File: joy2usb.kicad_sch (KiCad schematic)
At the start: 16 parts, among them J1 DB9_Male, J2 Conn_02x04_Odd_Even, SW1 RST, SW2 SW_SPDT, U1 Arduino_Pro_Micro, U2 4066

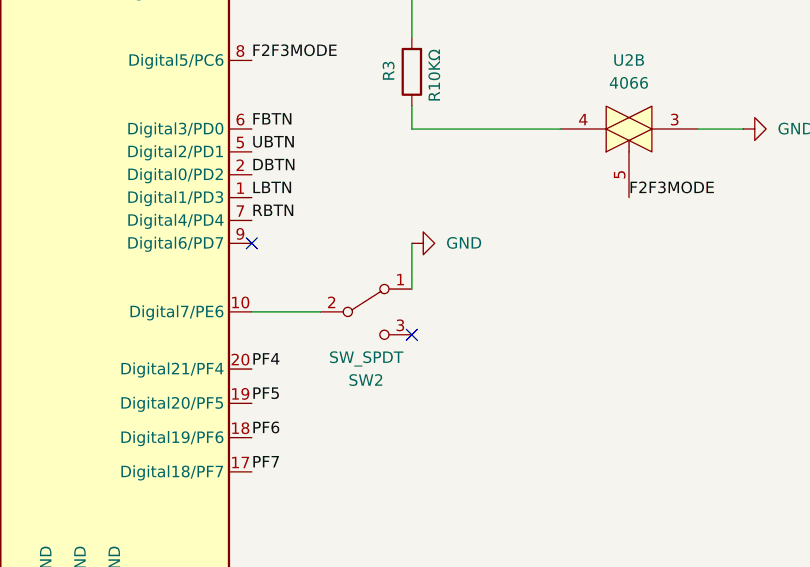
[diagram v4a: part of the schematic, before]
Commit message: PCB Rev. 4.0
update C64/Amiga switch
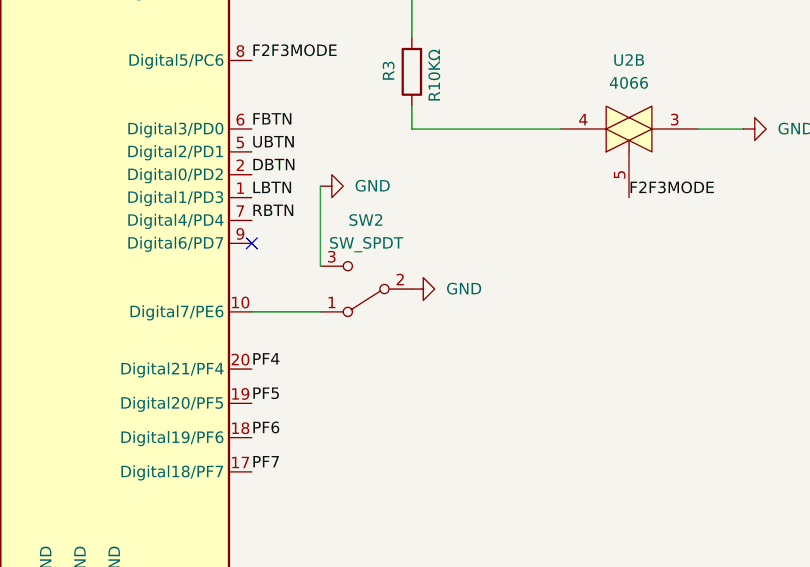
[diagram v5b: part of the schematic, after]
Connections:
- net GND: now also SW2.2 (B), SW2.3 (C); no longer SW2.1 (A)
- net at U1.10 (Digital7/PE6): now also SW2.1 (A); no longer SW2.2 (B)
- no-connect marks 7 -> 6
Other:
- moved on the sheet: SW2
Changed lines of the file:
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@@
   (title_block
     (title "joy2usb")
-    (rev "3.0")
+    (rev "4.0")
     (company "mistepien@wp.pl")
   )
@@
   (no_connect (at 111.76 55.88))
   (no_connect (at 111.76 91.44))
-  (no_connect (at 129.54 101.6))
   (no_connect (at 111.76 58.42))
   (no_connect (at 81.28 55.88))
@@
     (stroke (width 0) (type default) (color 0 0 0 0))
   )
-  (wire (pts (xy 129.54 91.44) (xy 129.54 96.52))
-    (stroke (width 0) (type default) (color 0 0 0 0))
-  )
   (wire (pts (xy 211.455 106.045) (xy 212.725 106.045))
     (stroke (width 0) (type default) (color 0 0 0 0))
@@
   )
   (wire (pts (xy 220.345 106.045) (xy 225.425 106.045))
+    (stroke (width 0) (type default) (color 0 0 0 0))
+  )
+  (wire (pts (xy 119.38 85.09) (xy 119.38 93.98))
     (stroke (width 0) (type default) (color 0 0 0 0))
   )
@@
     (pin "1")
   )
-  (symbol (lib_id "power:GND") (at 129.54 91.44 90) (unit 1)
-    (in_bom yes) (on_board yes) (fields_autoplaced)
-    (property "Reference" "#PWR0107" (id 0) (at 135.89 91.44 0)
-      (effects (font (size 1.27 1.27)) hide)
-    )
-    (property "Value" "GND" (id 1) (at 133.35 91.4399 90)
-      (effects (font (size 1.27 1.27)) (justify right))
-    )
-    (property "Footprint" "" (id 2) (at 129.54 91.44 0)
-      (effects (font (size 1.27 1.27)) hide)
-    )
-    (property "Datasheet" "" (id 3) (at 129.54 91.44 0)
-      (effects (font (size 1.27 1.27)) hide)
-    )
-    (pin "1")
-  )
   (symbol (lib_id "Mechanical:MountingHole") (at 137.795 181.61 0) (unit 1)
     (in_bom no) (on_board yes)
@@
     (pin "1")
   )
-  (symbol (lib_id "Switch:SW_SPDT") (at 124.46 99.06 0) (unit 1)
-    (in_bom yes) (on_board yes) (fields_autoplaced)
-    (property "Reference" "SW2" (id 0) (at 124.46 106.68 0))
-    (property "Value" "SW_SPDT" (id 1) (at 124.46 104.14 0))
-    (property "Footprint" "Misc:MFP_1220_KNITTER_SWITCH_SPDT_Oval" (id 2) (at 124.46 99.06 0)
-      (effects (font (size 1.27 1.27)) hide)
-    )
-    (property "Datasheet" "~" (id 3) (at 124.46 99.06 0)
+  (symbol (lib_id "Switch:SW_SPDT") (at 124.46 96.52 180) (unit 1)
+    (in_bom yes) (on_board yes) (fields_autoplaced)
+    (property "Reference" "SW2" (id 0) (at 124.46 88.9 0))
+    (property "Value" "SW_SPDT" (id 1) (at 124.46 91.44 0))
+    (property "Footprint" "Misc:MFP_1220_KNITTER_SWITCH_SPDT_Oval" (id 2) (at 124.46 96.52 0)
+      (effects (font (size 1.27 1.27)) hide)
+    )
+    (property "Datasheet" "~" (id 3) (at 124.46 96.52 0)
       (effects (font (size 1.27 1.27)) hide)
     )
@@
     (pin "1")
   )
-  (symbol (lib_id "power:VCC") (at 133.35 180.34 0) (unit 1)
-    (in_bom yes) (on_board yes) (fields_autoplaced)
-    (property "Reference" "#PWR023" (id 0) (at 133.35 184.15 0)
-      (effects (font (size 1.27 1.27)) hide)
-    )
-    (property "Value" "VCC" (id 1) (at 133.35 175.26 0))
-    (property "Footprint" "" (id 2) (at 133.35 180.34 0)
-      (effects (font (size 1.27 1.27)) hide)
-    )
-    (property "Datasheet" "" (id 3) (at 133.35 180.34 0)
-      (effects (font (size 1.27 1.27)) hide)
-    )
-    (pin "1")
-  )
   (symbol (lib_id "Device:LED") (at 216.535 106.045 180) (unit 1)
     (in_bom yes) (on_board yes) (fields_autoplaced)
@@
     )
     (property "Datasheet" "" (id 3) (at 92.71 137.16 0)
+      (effects (font (size 1.27 1.27)) hide)
+    )
+    (pin "1")
+  )
+  (symbol (lib_id "power:GND") (at 129.54 96.52 90) (unit 1)
+    (in_bom yes) (on_board yes) (fields_autoplaced)
+    (property "Reference" "#PWR0107" (id 0) (at 135.89 96.52 0)
+      (effects (font (size 1.27 1.27)) hide)
+    )
+    (property "Value" "GND" (id 1) (at 133.35 96.5199 90)
+      (effects (font (size 1.27 1.27)) (justify right))
+    )
+    (property "Footprint" "" (id 2) (at 129.54 96.52 0)
+      (effects (font (size 1.27 1.27)) hide)
+    )
+    (property "Datasheet" "" (id 3) (at 129.54 96.52 0)
       (effects (font (size 1.27 1.27)) hide)
     )
@@
     (pin "8")
   )
+  (symbol (lib_id "power:GND") (at 119.38 85.09 90) (unit 1)
+    (in_bom yes) (on_board yes) (fields_autoplaced)
+    (property "Reference" "#PWR02" (id 0) (at 125.73 85.09 0)
+      (effects (font (size 1.27 1.27)) hide)
+    )
+    (property "Value" "GND" (id 1) (at 123.19 85.0899 90)
+      (effects (font (size 1.27 1.27)) (justify right))
+    )
+    (property "Footprint" "" (id 2) (at 119.38 85.09 0)
+      (effects (font (size 1.27 1.27)) hide)
+    )
+    (property "Datasheet" "" (id 3) (at 119.38 85.09 0)
+      (effects (font (size 1.27 1.27)) hide)
+    )
+    (pin "1")
+  )
   (symbol (lib_id "power:GND") (at 33.02 128.27 180) (unit 1)
     (in_bom yes) (on_board yes) (fields_autoplaced)
@@
     )
   )
+  (symbol (lib_id "power:VCC") (at 133.35 180.34 0) (unit 1)
+    (in_bom yes) (on_board yes) (fields_autoplaced)
+    (property "Reference" "#PWR0117" (id 0) (at 133.35 184.15 0)
+      (effects (font (size 1.27 1.27)) hide)
+    )
+    (property "Value" "VCC" (id 1) (at 133.35 175.26 0))
+    (property "Footprint" "" (id 2) (at 133.35 180.34 0)
+      (effects (font (size 1.27 1.27)) hide)
+    )
+    (property "Datasheet" "" (id 3) (at 133.35 180.34 0)
+      (effects (font (size 1.27 1.27)) hide)
+    )
+    (pin "1")
+  )
   (symbol (lib_id "Mechanical:MountingHole") (at 137.795 190.5 0) (unit 1)
     (in_bom no) (on_board yes)
@@
       (reference "#PWR01") (unit 1) (value "VCC") (footprint "")
     )
+    (path "/b360e194-d5b5-4145-87b4-c475cf3ef423"
+      (reference "#PWR02") (unit 1) (value "GND") (footprint "")
+    )
     (path "/9b6d3cc9-8699-4512-8b17-ada5ebf54a78"
       (reference "#PWR03") (unit 1) (value "VCC") (footprint "")
@@
       (reference "#PWR017") (unit 1) (value "VCC") (footprint "")
     )
-    (path "/3df7e21b-5810-4bcd-8937-5da3a9ffe577"
-      (reference "#PWR023") (unit 1) (value "VCC") (footprint "")
-    )
     (path "/0826918b-c24e-40db-a768-35c3e120095f"
       (reference "#PWR0101") (unit 1) (value "VCC") (footprint "")
@@
       (reference "#PWR0106") (unit 1) (value "GND") (footprint "")
     )
-    (path "/084083df-fdf8-459b-b91f-12f5dfdc3fca"
+    (path "/53eb5098-0697-4345-8a1e-de4578279585"
       (reference "#PWR0107") (unit 1) (value "GND") (footprint "")
     )
@@
       (reference "#PWR0116") (unit 1) (value "GND") (footprint "")
     )
+    (path "/c125f043-00b6-4dfd-8738-0b01be89b4c8"
+      (reference "#PWR0117") (unit 1) (value "VCC") (footprint "")
+    )
     (path "/fed0e2ac-5eb0-44b8-8f14-4abe77bb9479"

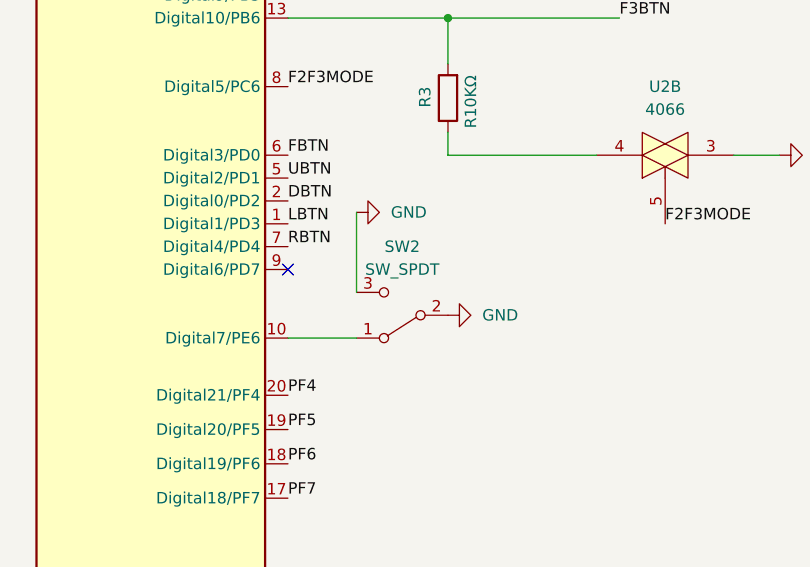
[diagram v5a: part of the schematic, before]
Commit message: PCB Rev. 4.1
SW2 minor amendment
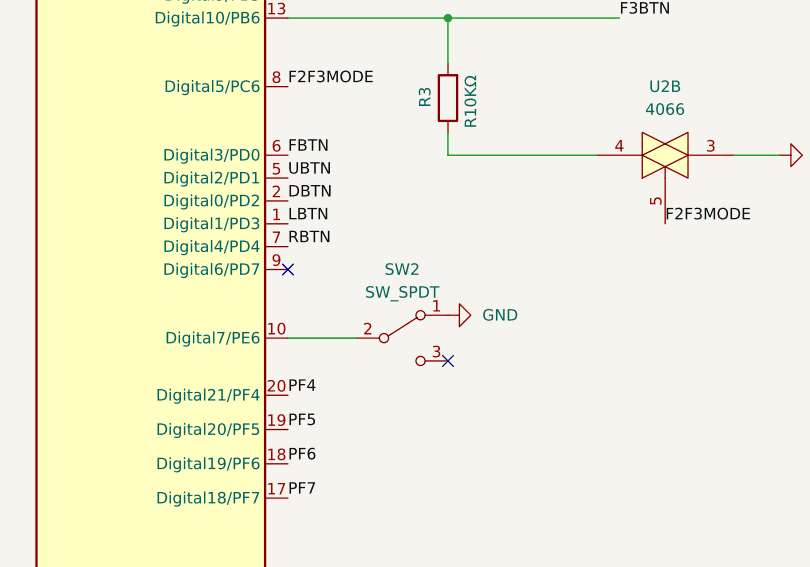
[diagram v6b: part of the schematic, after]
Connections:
- net GND: now also SW2.1 (A); no longer SW2.2 (B), SW2.3 (C)
- net at U1.10 (Digital7/PE6): now also SW2.2 (B); no longer SW2.1 (A)
- no-connect marks 6 -> 7
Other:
- moved on the sheet: SW2
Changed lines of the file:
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@@
   (title_block
     (title "joy2usb")
-    (rev "4.0")
+    (rev "4.1")
     (company "mistepien@wp.pl")
   )
@@
   (no_connect (at 81.28 55.88))
   (no_connect (at 111.76 50.8))
+  (no_connect (at 129.54 101.6))
   (wire (pts (xy 231.14 48.26) (xy 238.76 48.26))
     (stroke (width 0) (type default) (color 0 0 0 0))
@@
   )
   (wire (pts (xy 220.345 106.045) (xy 225.425 106.045))
-    (stroke (width 0) (type default) (color 0 0 0 0))
-  )
-  (wire (pts (xy 119.38 85.09) (xy 119.38 93.98))
     (stroke (width 0) (type default) (color 0 0 0 0))
   )
@@
     (pin "1")
   )
-  (symbol (lib_id "Switch:SW_SPDT") (at 124.46 96.52 180) (unit 1)
-    (in_bom yes) (on_board yes) (fields_autoplaced)
-    (property "Reference" "SW2" (id 0) (at 124.46 88.9 0))
-    (property "Value" "SW_SPDT" (id 1) (at 124.46 91.44 0))
-    (property "Footprint" "Misc:MFP_1220_KNITTER_SWITCH_SPDT_Oval" (id 2) (at 124.46 96.52 0)
-      (effects (font (size 1.27 1.27)) hide)
-    )
-    (property "Datasheet" "~" (id 3) (at 124.46 96.52 0)
+  (symbol (lib_id "Switch:SW_SPDT") (at 124.46 99.06 0) (unit 1)
+    (in_bom yes) (on_board yes) (fields_autoplaced)
+    (property "Reference" "SW2" (id 0) (at 124.46 91.44 0))
+    (property "Value" "SW_SPDT" (id 1) (at 124.46 93.98 0))
+    (property "Footprint" "Misc:MFP_1220_KNITTER_SWITCH_SPDT_Oval" (id 2) (at 124.46 99.06 0)
+      (effects (font (size 1.27 1.27)) hide)
+    )
+    (property "Datasheet" "~" (id 3) (at 124.46 99.06 0)
       (effects (font (size 1.27 1.27)) hide)
     )
@@
     (pin "8")
   )
-  (symbol (lib_id "power:GND") (at 119.38 85.09 90) (unit 1)
-    (in_bom yes) (on_board yes) (fields_autoplaced)
-    (property "Reference" "#PWR02" (id 0) (at 125.73 85.09 0)
-      (effects (font (size 1.27 1.27)) hide)
-    )
-    (property "Value" "GND" (id 1) (at 123.19 85.0899 90)
-      (effects (font (size 1.27 1.27)) (justify right))
-    )
-    (property "Footprint" "" (id 2) (at 119.38 85.09 0)
-      (effects (font (size 1.27 1.27)) hide)
-    )
-    (property "Datasheet" "" (id 3) (at 119.38 85.09 0)
-      (effects (font (size 1.27 1.27)) hide)
-    )
-    (pin "1")
-  )
   (symbol (lib_id "power:GND") (at 33.02 128.27 180) (unit 1)
     (in_bom yes) (on_board yes) (fields_autoplaced)
@@
       (reference "#PWR01") (unit 1) (value "VCC") (footprint "")
     )
-    (path "/b360e194-d5b5-4145-87b4-c475cf3ef423"
-      (reference "#PWR02") (unit 1) (value "GND") (footprint "")
-    )
     (path "/9b6d3cc9-8699-4512-8b17-ada5ebf54a78"

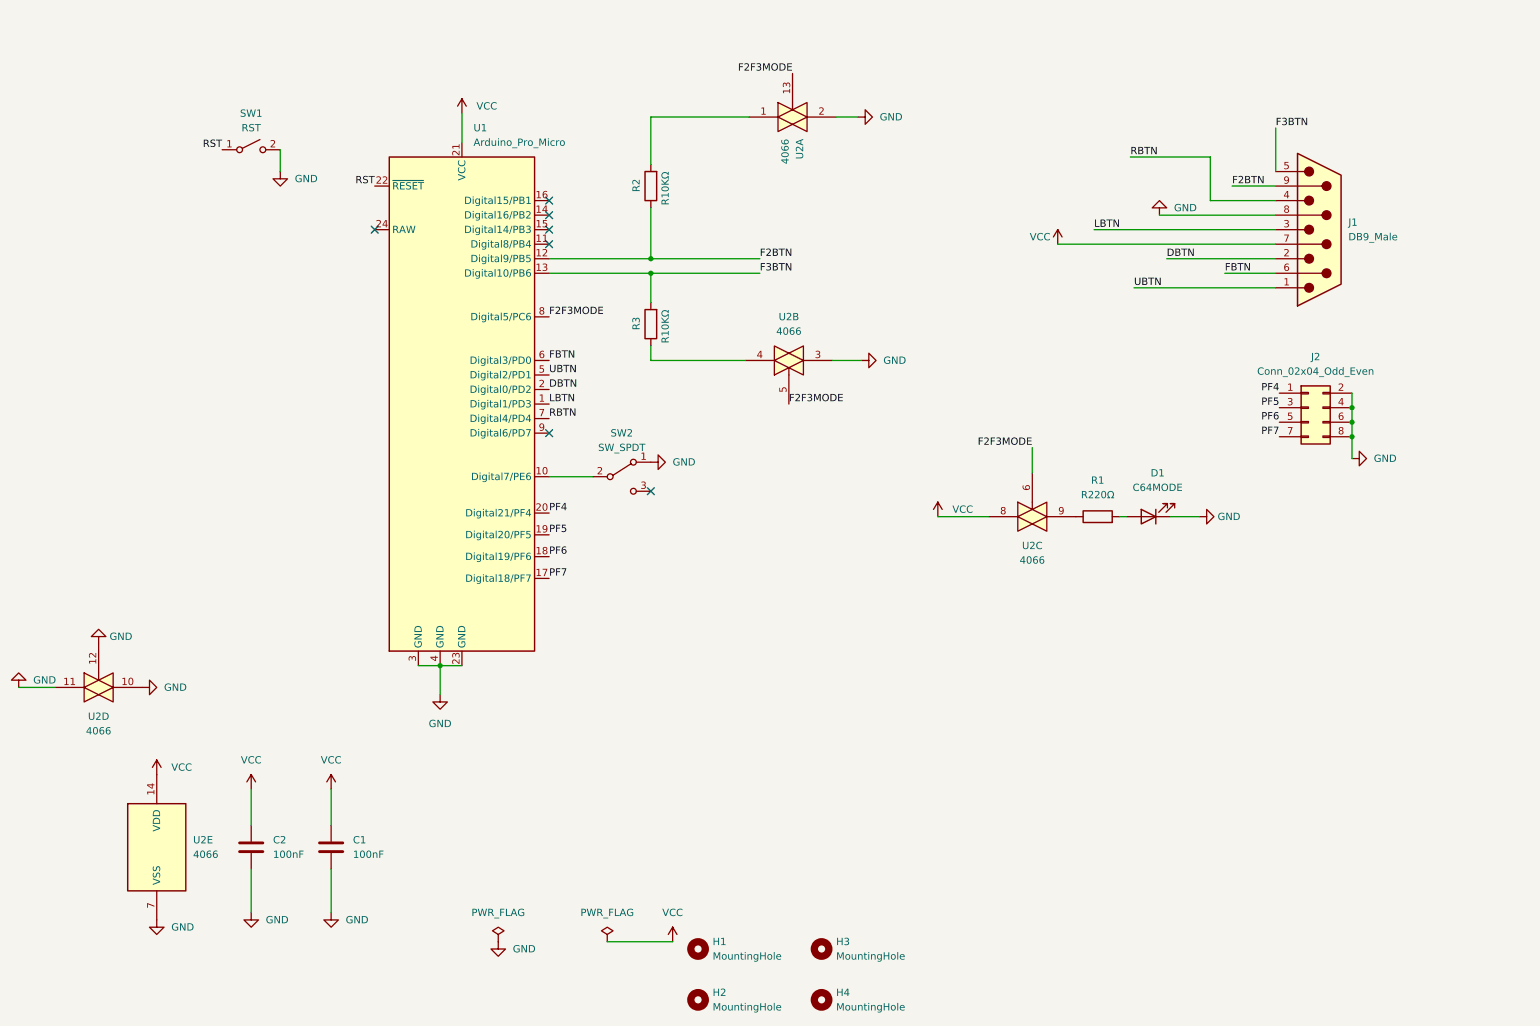
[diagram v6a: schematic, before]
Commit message: PCB Rev. 5.0
Minor update of DB9 socket footprint.
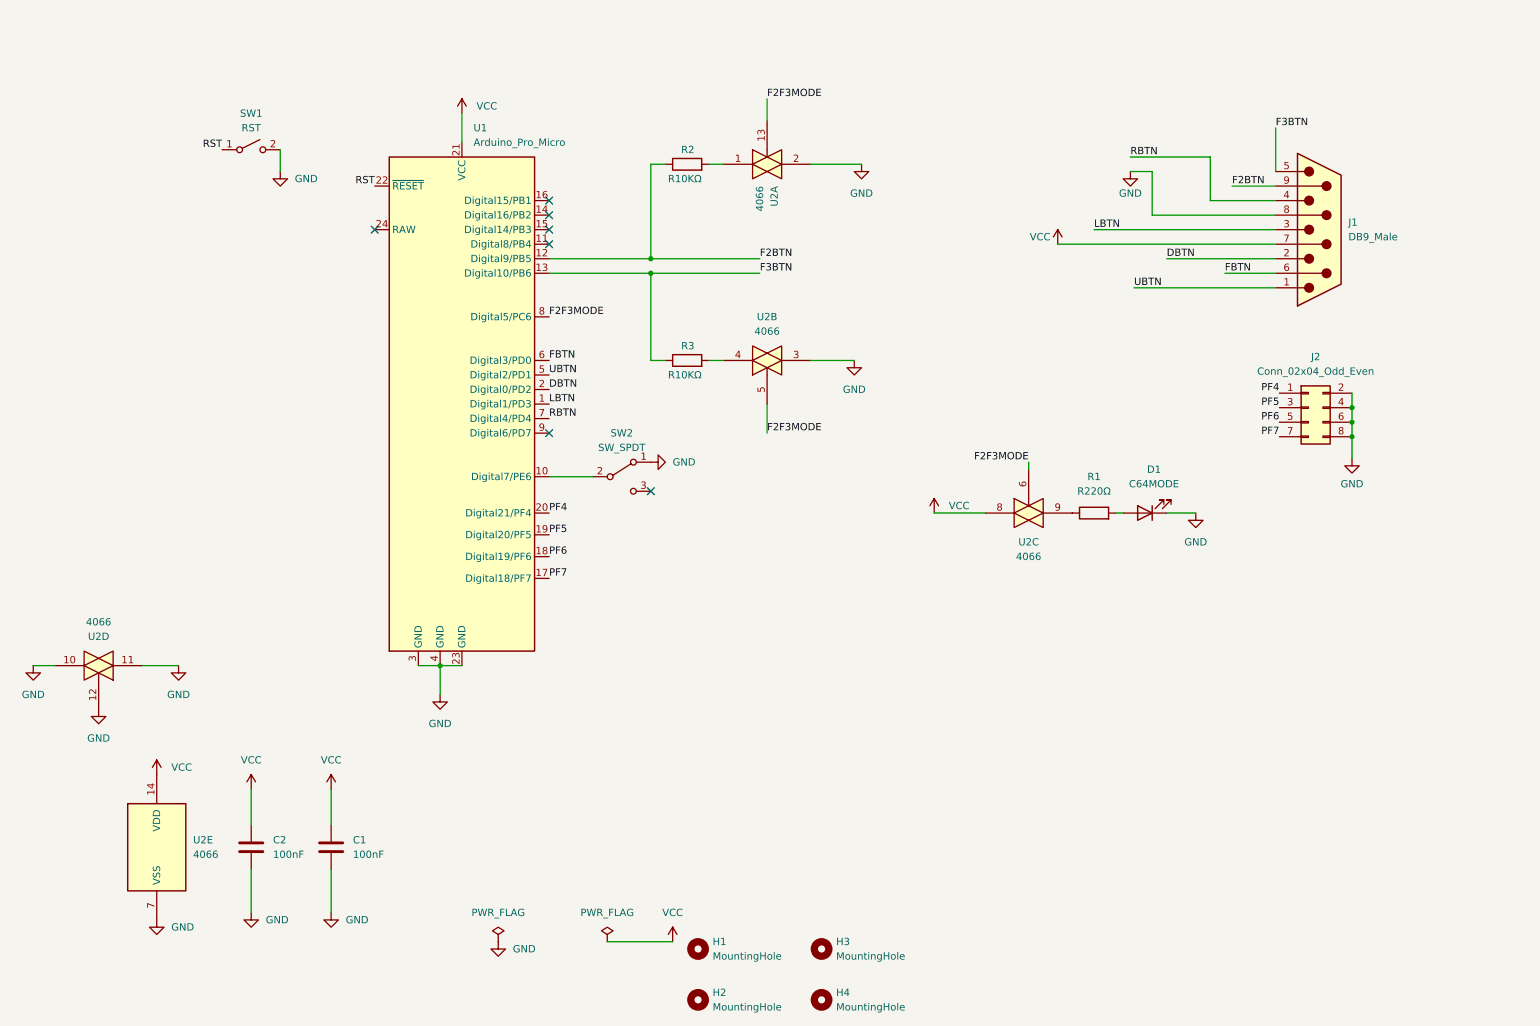
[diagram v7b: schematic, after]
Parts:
- J1: footprint Misc:DSUB-9_Male_Horizontal_P2.77x2.84mm_EdgePinOffset9.90mm_Housed_OVAL_MountingHolesOffset11.32mm -> misc:DSUB-9_Male_Horizontal_P2.77x2.84mm_EdgePinOffset9.90mm_Housed_OVAL_MountingHolesOffset11.32mm
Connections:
- net F3BTN: now also R3.1; no longer R3.2
- net at U2.4: now also R3.2; no longer R3.1
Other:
- moved on the sheet: D1, R1, R2, R3, U2A, U2B, U2C, U2D
